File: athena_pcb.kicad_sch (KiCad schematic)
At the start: 36 parts, among them J2 Conn_01x04, SW1 SW_Push, U1 NRF5340-QKAA-R7, U2 BME280, Y1 32MHz, Y2 32.768kHz

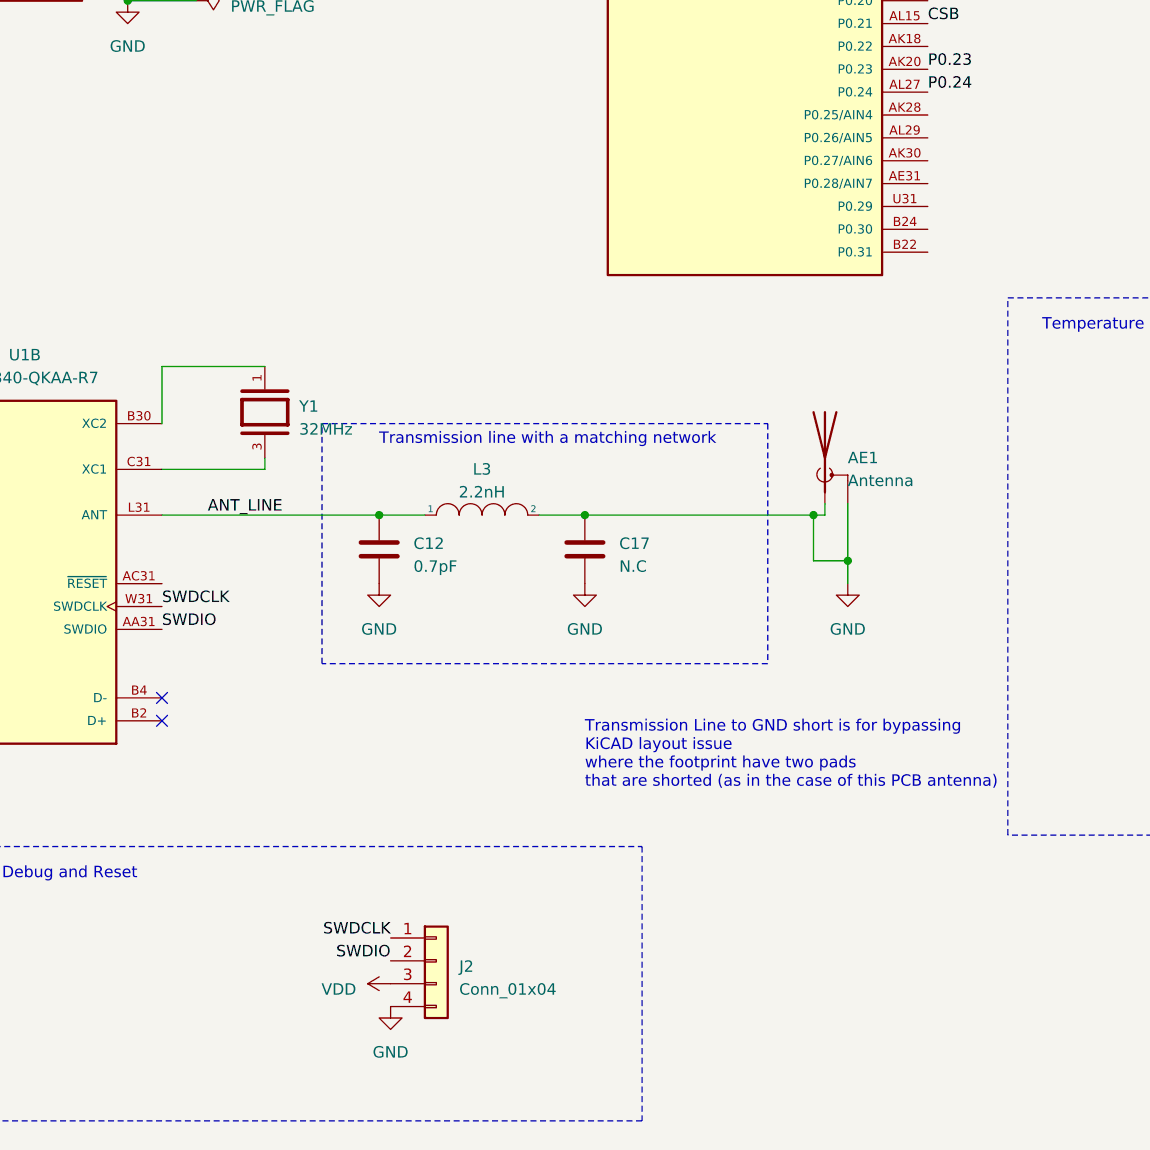
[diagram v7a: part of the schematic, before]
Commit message: Updated Header pinout, added ground pours to PCB
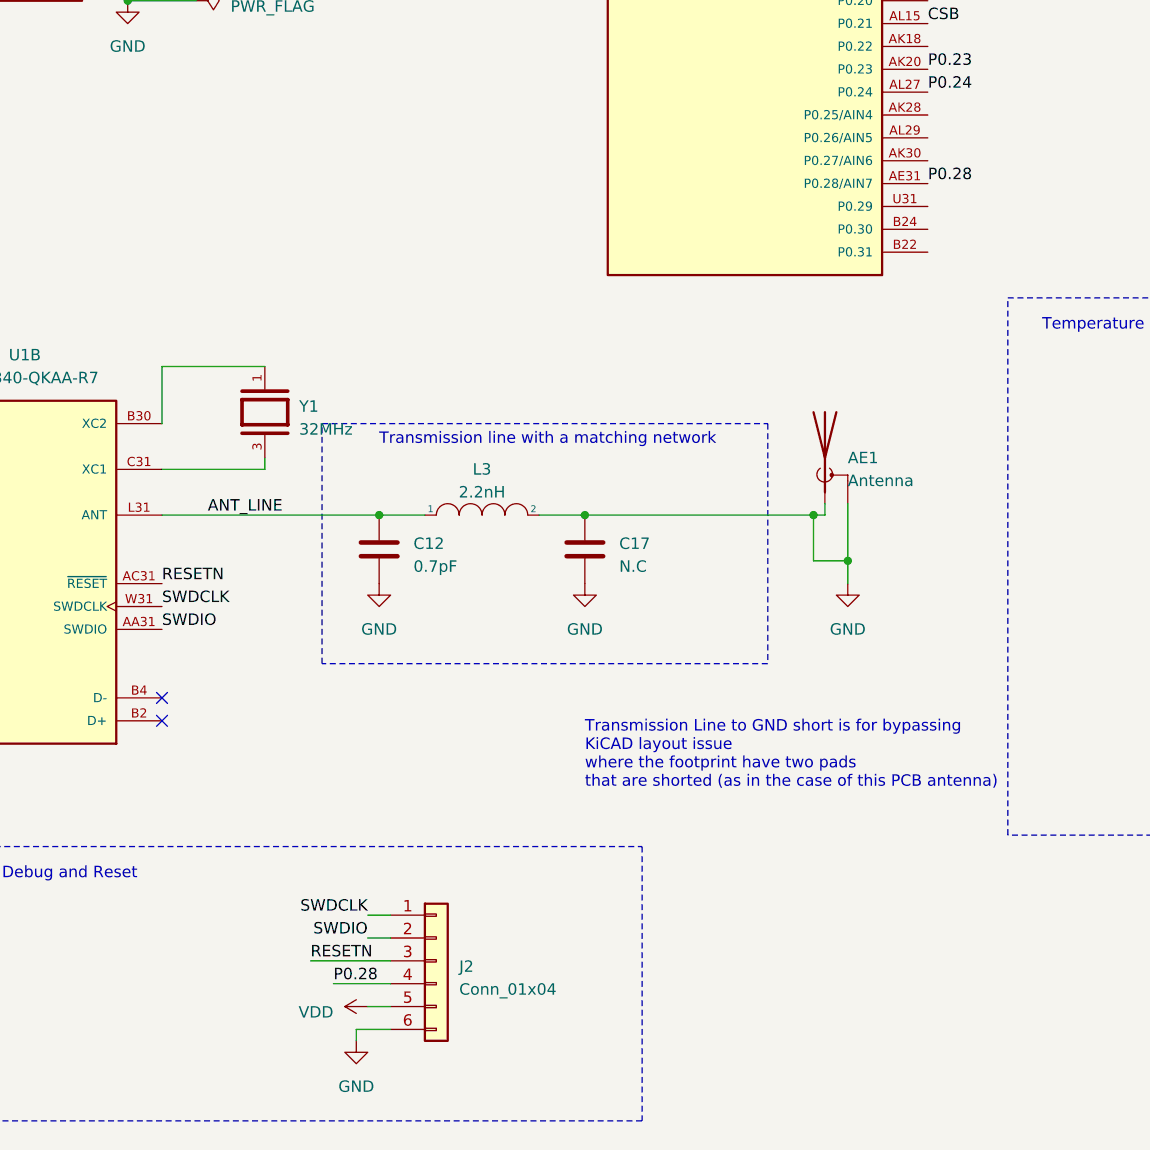
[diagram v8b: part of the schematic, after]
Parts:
- J2: footprint Connector_PinSocket_1.27mm:PinSocket_1x04_P1.27mm_Vertical -> Connector_PinSocket_1.27mm:PinSocket_1x06_P1.27mm_Vertical; symbol Connector_Generic:Conn_01x04 -> Connector_Generic:Conn_01x06
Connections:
- net GND: now also J2.6 (Pin_6); no longer J2.4 (Pin_4)
- net VDD: now also J2.5 (Pin_5); no longer J2.3 (Pin_3)
- net P0.28: now reaches U1.AE31 (P0.28/AIN7)
- net P0.28: now also J2.4 (Pin_4)
- net RESETN: now reaches U1.AC31 (~{RESET})
- net RESETN: now also J2.3 (Pin_3)
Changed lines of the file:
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@@
   (no_connect (at 115.57 148.59))
   (no_connect (at 115.57 151.13))
+  (wire (pts (xy 138.43 182.88) (xy 140.97 182.88))
+    (stroke (width 0) (type default))
+  )
   (wire (pts (xy 200.66 22.86) (xy 217.17 22.86))
     (stroke (width 0) (type default))
@@
     (stroke (width 0) (type default))
   )
+  (wire (pts (xy 134.62 180.34) (xy 140.97 180.34))
+    (stroke (width 0) (type default))
+  )
   (wire (pts (xy 187.96 133.35) (xy 191.77 133.35))
     (stroke (width 0) (type default))
@@
     (stroke (width 0) (type default))
   )
+  (wire (pts (xy 132.08 177.8) (xy 140.97 177.8))
+    (stroke (width 0) (type default))
+  )
   (wire (pts (xy 111.76 27.94) (xy 111.76 35.56))
     (stroke (width 0) (type default))
@@
     (stroke (width 0) (type default))
   )
+  (wire (pts (xy 140.97 185.42) (xy 137.16 185.42))
+    (stroke (width 0) (type default))
+  )
   (wire (pts (xy 31.75 101.6) (xy 31.75 104.14))
     (stroke (width 0) (type default))
@@
     (stroke (width 0) (type default))
   )
+  (wire (pts (xy 137.16 185.42) (xy 137.16 186.69))
+    (stroke (width 0) (type default))
+  )
   (wire (pts (xy 232.41 85.09) (xy 228.6 85.09))
     (stroke (width 0) (type default))
@@
     (stroke (width 0) (type default))
   )
+  (wire (pts (xy 138.43 172.72) (xy 140.97 172.72))
+    (stroke (width 0) (type default))
+  )
   (wire (pts (xy 20.32 25.4) (xy 20.32 27.94))
     (stroke (width 0) (type default))
@@
   )
   (wire (pts (xy 127 123.19) (xy 115.57 123.19))
+    (stroke (width 0) (type default))
+  )
+  (wire (pts (xy 138.43 175.26) (xy 140.97 175.26))
     (stroke (width 0) (type default))
   )
@@
     (effects (font (size 1.27 1.27)) (justify left bottom))
   )
+  (label "P0.28" (at 134.62 180.34 0) (fields_autoplaced)
+    (effects (font (size 1.27 1.27)) (justify left bottom))
+  )
   (label "SDO" (at 265.43 129.54 0) (fields_autoplaced)
     (effects (font (size 1.27 1.27)) (justify left bottom))
@@
     (effects (font (size 1.27 1.27)) (justify left bottom))
   )
-  (label "SWDIO" (at 140.97 177.8 180) (fields_autoplaced)
+  (label "RESETN" (at 115.57 135.89 0) (fields_autoplaced)
+    (effects (font (size 1.27 1.27)) (justify left bottom))
+  )
+  (label "SWDIO" (at 138.43 175.26 180) (fields_autoplaced)
     (effects (font (size 1.27 1.27)) (justify right bottom))
   )
@@
     (effects (font (size 1.27 1.27)) (justify left bottom))
   )
-  (label "SWDCLK" (at 140.97 175.26 180) (fields_autoplaced)
+  (label "SWDCLK" (at 138.43 172.72 180) (fields_autoplaced)
     (effects (font (size 1.27 1.27)) (justify right bottom))
   )
@@
     (effects (font (size 1.27 1.27)) (justify left bottom))
   )
+  (label "RESETN" (at 132.08 177.8 0) (fields_autoplaced)
+    (effects (font (size 1.27 1.27)) (justify left bottom))
+  )
   (label "VBAT_sense" (at 39.37 101.6 0) (fields_autoplaced)
+    (effects (font (size 1.27 1.27)) (justify left bottom))
+  )
+  (label "P0.28" (at 200.66 91.44 0) (fields_autoplaced)
     (effects (font (size 1.27 1.27)) (justify left bottom))
   )
@@
         (path "/fadb6411-1081-41a3-ba72-837bcce93ee0"
           (reference "#PWR028") (unit 1)
-        )
-      )
-    )
-  )
-  (symbol (lib_id "power:VDD") (at 140.97 180.34 90) (unit 1)
-    (in_bom yes) (on_board yes) (dnp no) (fields_autoplaced)
-    (property "Reference" "#PWR037" (at 144.78 180.34 0)
-      (effects (font (size 1.27 1.27)) hide)
-    )
-    (property "Value" "VDD" (at 137.16 180.975 90)
-      (effects (font (size 1.27 1.27)) (justify left))
-    )
-    (property "Footprint" "" (at 140.97 180.34 0)
-      (effects (font (size 1.27 1.27)) hide)
-    )
-    (property "Datasheet" "" (at 140.97 180.34 0)
-      (effects (font (size 1.27 1.27)) hide)
-    )
-    (pin "1")
-    (instances
-      (project "athena_pcb"
-        (path "/fadb6411-1081-41a3-ba72-837bcce93ee0"
-          (reference "#PWR037") (unit 1)
         )
       )
@@
     )
   )
+  (symbol (lib_id "power:VDD") (at 138.43 182.88 90) (unit 1)
+    (in_bom yes) (on_board yes) (dnp no) (fields_autoplaced)
+    (property "Reference" "#PWR09" (at 142.24 182.88 0)
+      (effects (font (size 1.27 1.27)) hide)
+    )
+    (property "Value" "VDD" (at 134.62 183.515 90)
+      (effects (font (size 1.27 1.27)) (justify left))
+    )
+    (property "Footprint" "" (at 138.43 182.88 0)
+      (effects (font (size 1.27 1.27)) hide)
+    )
+    (property "Datasheet" "" (at 138.43 182.88 0)
+      (effects (font (size 1.27 1.27)) hide)
+    )
+    (pin "1")
+    (instances
+      (project "athena_pcb"
+        (path "/fadb6411-1081-41a3-ba72-837bcce93ee0"
+          (reference "#PWR09") (unit 1)
+        )
+      )
+    )
+  )
   (symbol (lib_id "power:VDD") (at 20.32 25.4 0) (unit 1)
     (in_bom yes) (on_board yes) (dnp no) (fields_autoplaced)
@@
     )
   )
-  (symbol (lib_id "Connector_Generic:Conn_01x04") (at 146.05 177.8 0) (unit 1)
+  (symbol (lib_id "Connector_Generic:Conn_01x06") (at 146.05 177.8 0) (unit 1)
     (in_bom yes) (on_board yes) (dnp no) (fields_autoplaced)
     (property "Reference" "J2" (at 148.59 178.435 0)
@@
       (effects (font (size 1.27 1.27)) (justify left))
     )
-    (property "Footprint" "Connector_PinSocket_1.27mm:PinSocket_1x04_P1.27mm_Vertical" (at 146.05 177.8 0)
+    (property "Footprint" "Connector_PinSocket_1.27mm:PinSocket_1x06_P1.27mm_Vertical" (at 146.05 177.8 0)
       (effects (font (size 1.27 1.27)) hide)
     )
@@
     (pin "3")
     (pin "4")
+    (pin "5")
+    (pin "6")
     (instances
       (project "athena_pcb"
@@
         (path "/fadb6411-1081-41a3-ba72-837bcce93ee0"
           (reference "C3") (unit 1)
-        )
-      )
-    )
-  )
-  (symbol (lib_id "power:GND") (at 140.97 182.88 0) (unit 1)
-    (in_bom yes) (on_board yes) (dnp no) (fields_autoplaced)
-    (property "Reference" "#PWR09" (at 140.97 189.23 0)
-      (effects (font (size 1.27 1.27)) hide)
-    )
-    (property "Value" "GND" (at 140.97 187.96 0)
-      (effects (font (size 1.27 1.27)))
-    )
-    (property "Footprint" "" (at 140.97 182.88 0)
-      (effects (font (size 1.27 1.27)) hide)
-    )
-    (property "Datasheet" "" (at 140.97 182.88 0)
-      (effects (font (size 1.27 1.27)) hide)
-    )
-    (pin "1")
-    (instances
-      (project "athena_pcb"
-        (path "/fadb6411-1081-41a3-ba72-837bcce93ee0"
-          (reference "#PWR09") (unit 1)
         )
       )
@@
         )
       )
+    )
+  )
+  (symbol (lib_id "power:GND") (at 137.16 186.69 0) (unit 1)
+    (in_bom yes) (on_board yes) (dnp no) (fields_autoplaced)
+    (property "Reference" "#PWR07" (at 137.16 193.04 0)
+      (effects (font (size 1.27 1.27)) hide)
+    )
+    (property "Value" "GND" (at 137.16 191.77 0)
+      (effects (font (size 1.27 1.27)))
+    )
+    (property "Footprint" "" (at 137.16 186.69 0)
+      (effects (font (size 1.27 1.27)) hide)
+    )
+    (property "Datasheet" "" (at 137.16 186.69 0)
+      (effects (font (size 1.27 1.27)) hide)
+    )
+    (pin "1")
+    (instances
+      (project "athena_pcb"
+        (path "/fadb6411-1081-41a3-ba72-837bcce93ee0"
+          (reference "#PWR07") (unit 1)
+        )
+      )
